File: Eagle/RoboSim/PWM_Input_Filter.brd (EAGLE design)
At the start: 74.6 x 78.7 mm, 66 parts, among them IC1 TLV2772, IC2 TLV2772, IC3 TLV2772

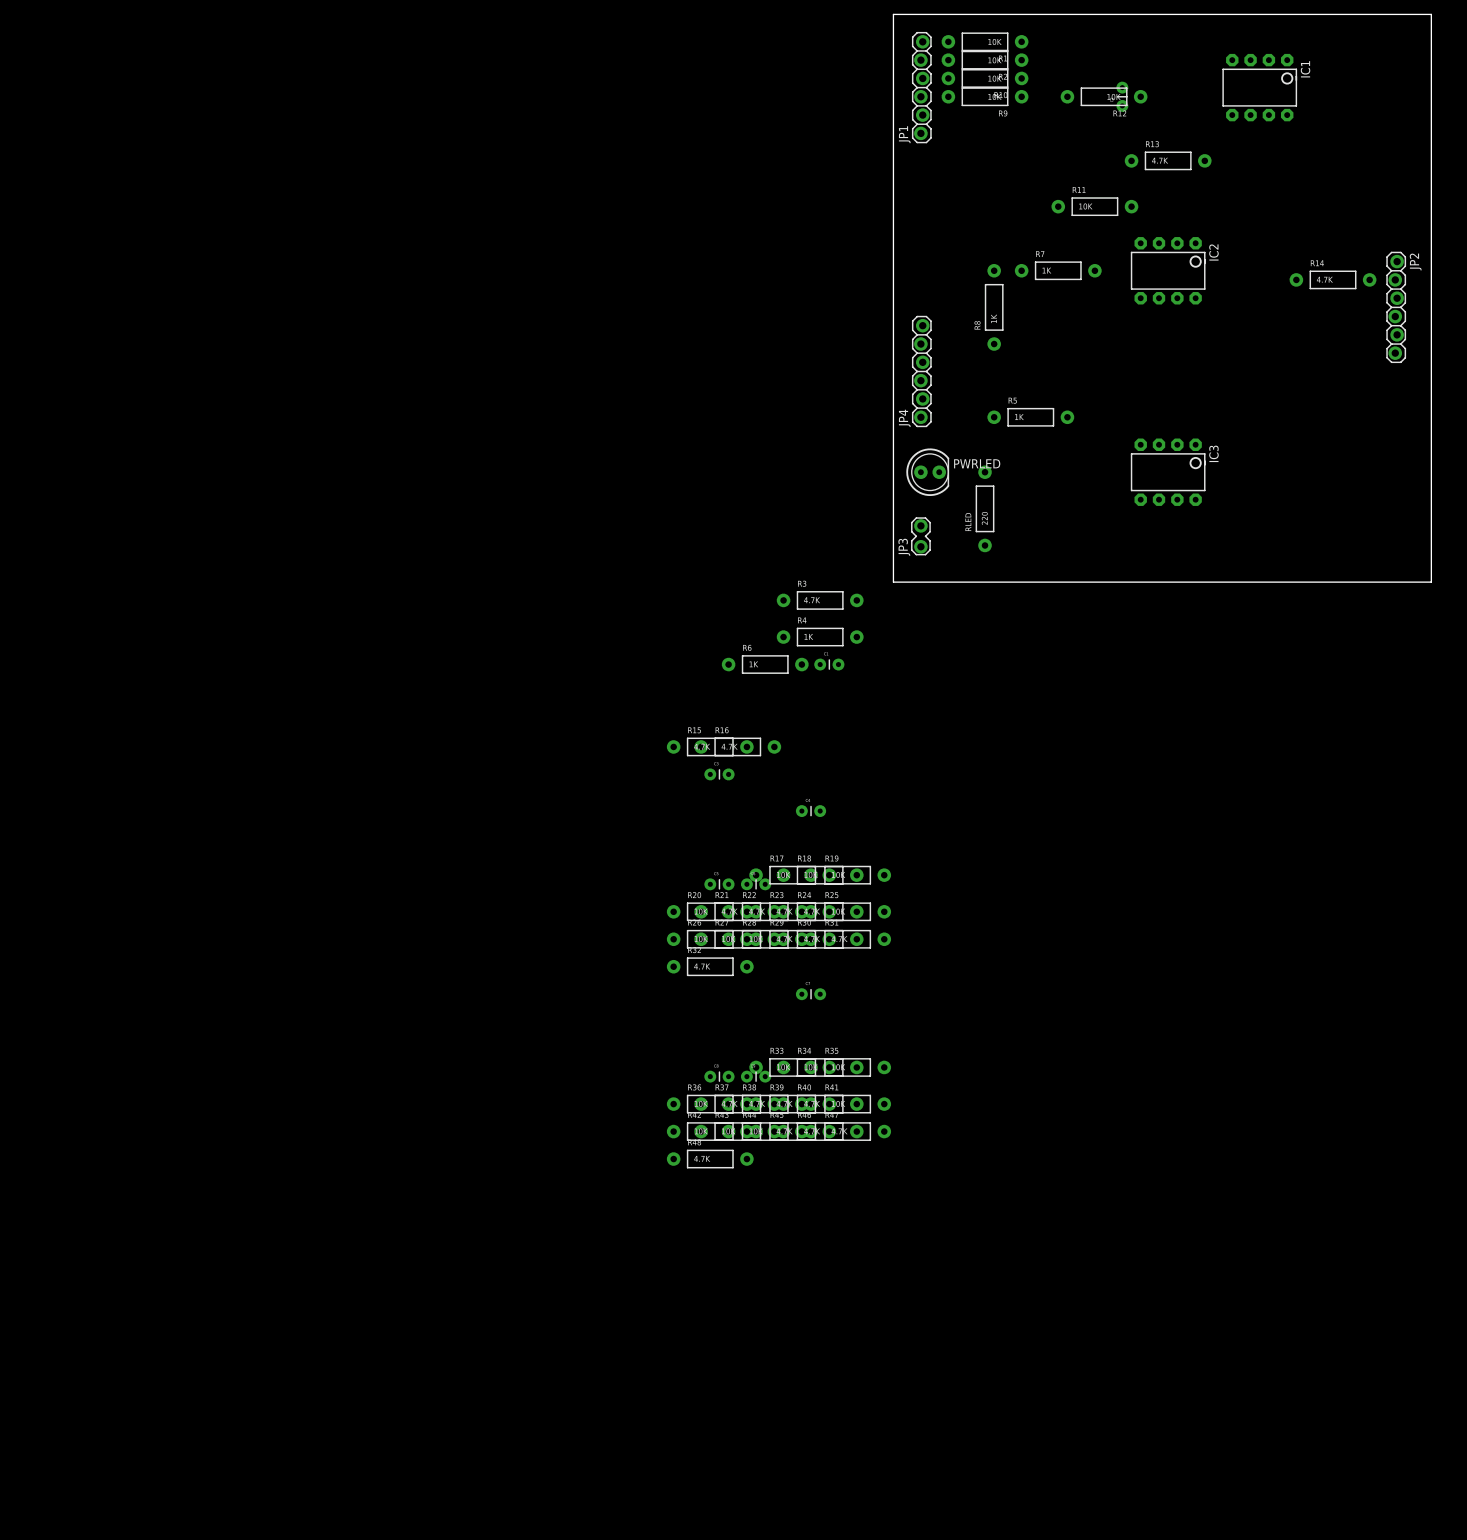
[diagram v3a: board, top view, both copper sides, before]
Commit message: updated resistor values and op-amp configuration
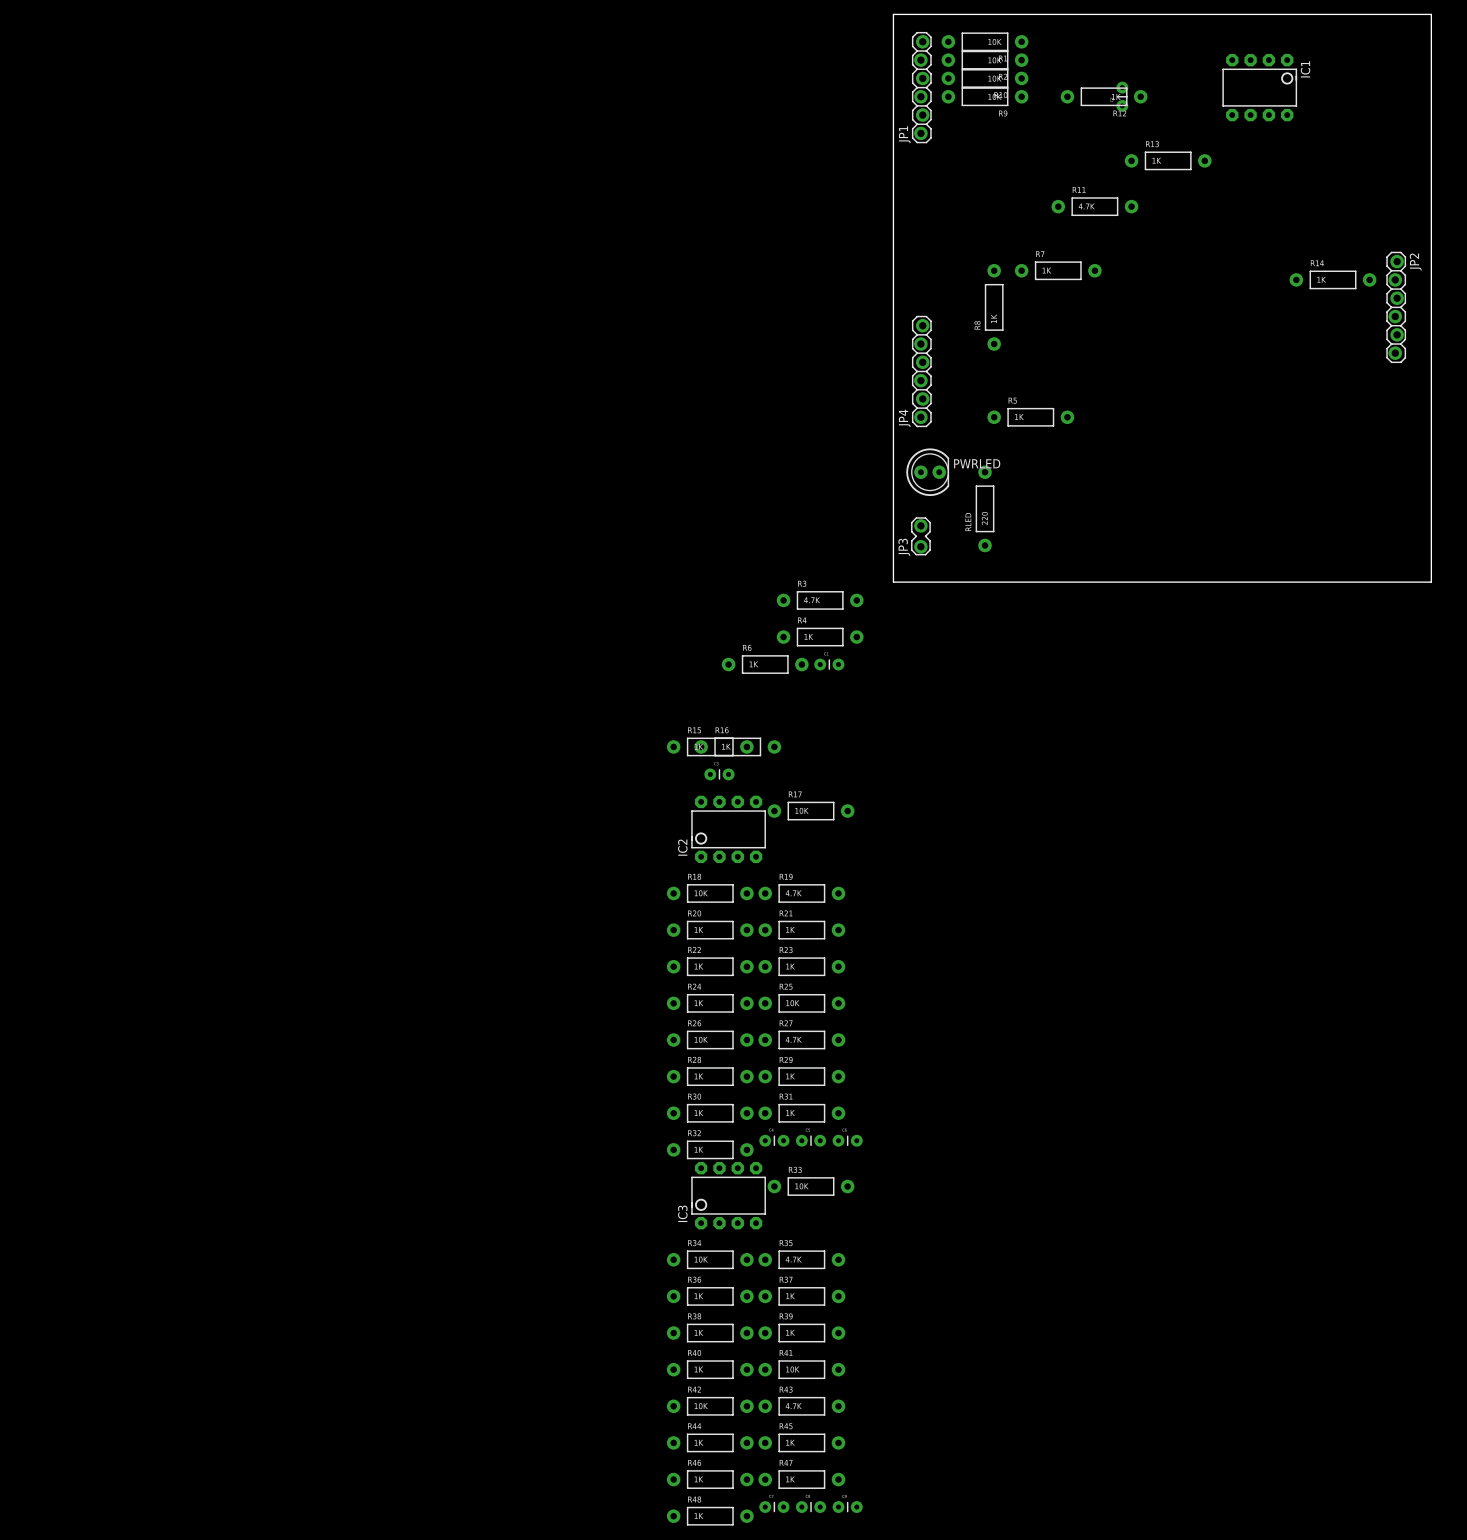
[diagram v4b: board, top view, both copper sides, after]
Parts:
- C2, C4, C7: value 100uF -> 3.7uF
- R11, R19, R27, R35, R43: value 10K -> 4.7K
- R12, R20, R28, R36, R44: value 10K -> 1K
- R13, R14, R15, R16, R21, R22, R23, R24, R29, R30, R31, R32, R37, R38, R39, R40, R45, R46, R47, R48: value 4.7K -> 1K
- moved IC3 117.4 mm to (-22.9, -85.1), turned to 0 degrees
- moved IC2 98.6 mm to (-22.9, -34.3), turned to 0 degrees
- moved C7 71.3 mm to (-17.8, -128.3)
- moved C8 61.0 mm to (-12.7, -128.3)
- moved C9 61.0 mm to (-7.62, -128.3)
- moved R46 50.6 mm to (-25.4, -124.5)
- moved R48 49.5 mm to (-25.4, -129.5)
- moved R47 48.7 mm to (-12.7, -124.5)
- moved C4 46.0 mm to (-17.8, -77.5)
- moved R44 43.8 mm to (-25.4, -119.4)
- moved R45 43.2 mm to (-12.7, -119.4)
- moved R40 39.9 mm to (-25.4, -109.2)
- moved R43 39.1 mm to (-12.7, -114.3)
- moved R42 38.1 mm to (-25.4, -114.3)
- moved C5 37.8 mm to (-12.7, -77.5)
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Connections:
- removed net N$26 (its old number): IC2.5, R26.P$1, R27.P$2, R29.P$1
- removed net N$27 (its old number): IC2.6, R25.P$1, R28.P$2, R31.P$2
- removed net N$32 (its old number): JP4.3, R33.P$2
- removed net N$40 (its old number): IC3.5, R42.P$1, R43.P$2, R45.P$1
- removed net N$41 (its old number): IC3.6, R41.P$1, R44.P$2, R47.P$2
- new net N$28: IC2.6, R26.P$1, R27.P$2, R29.P$1
- new net N$29: IC2.5, R25.P$1, R28.P$2, R31.P$2
- new net N$31: R33.P$2
- new net N$48: IC3.6, R42.P$1, R43.P$2, R45.P$1
- new net N$49: IC3.5, R41.P$1, R44.P$2, R47.P$2
- net N$11: now also IC1.6; no longer IC1.5
- net N$12: now also IC1.5; no longer IC1.6
- net N$16: now also R18.P$2; no longer R17.P$2
- net N$2: now also R17.P$2; no longer R18.P$2

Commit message: changed pins to screw terminals and made resistors surface mount. Still need to position components and route
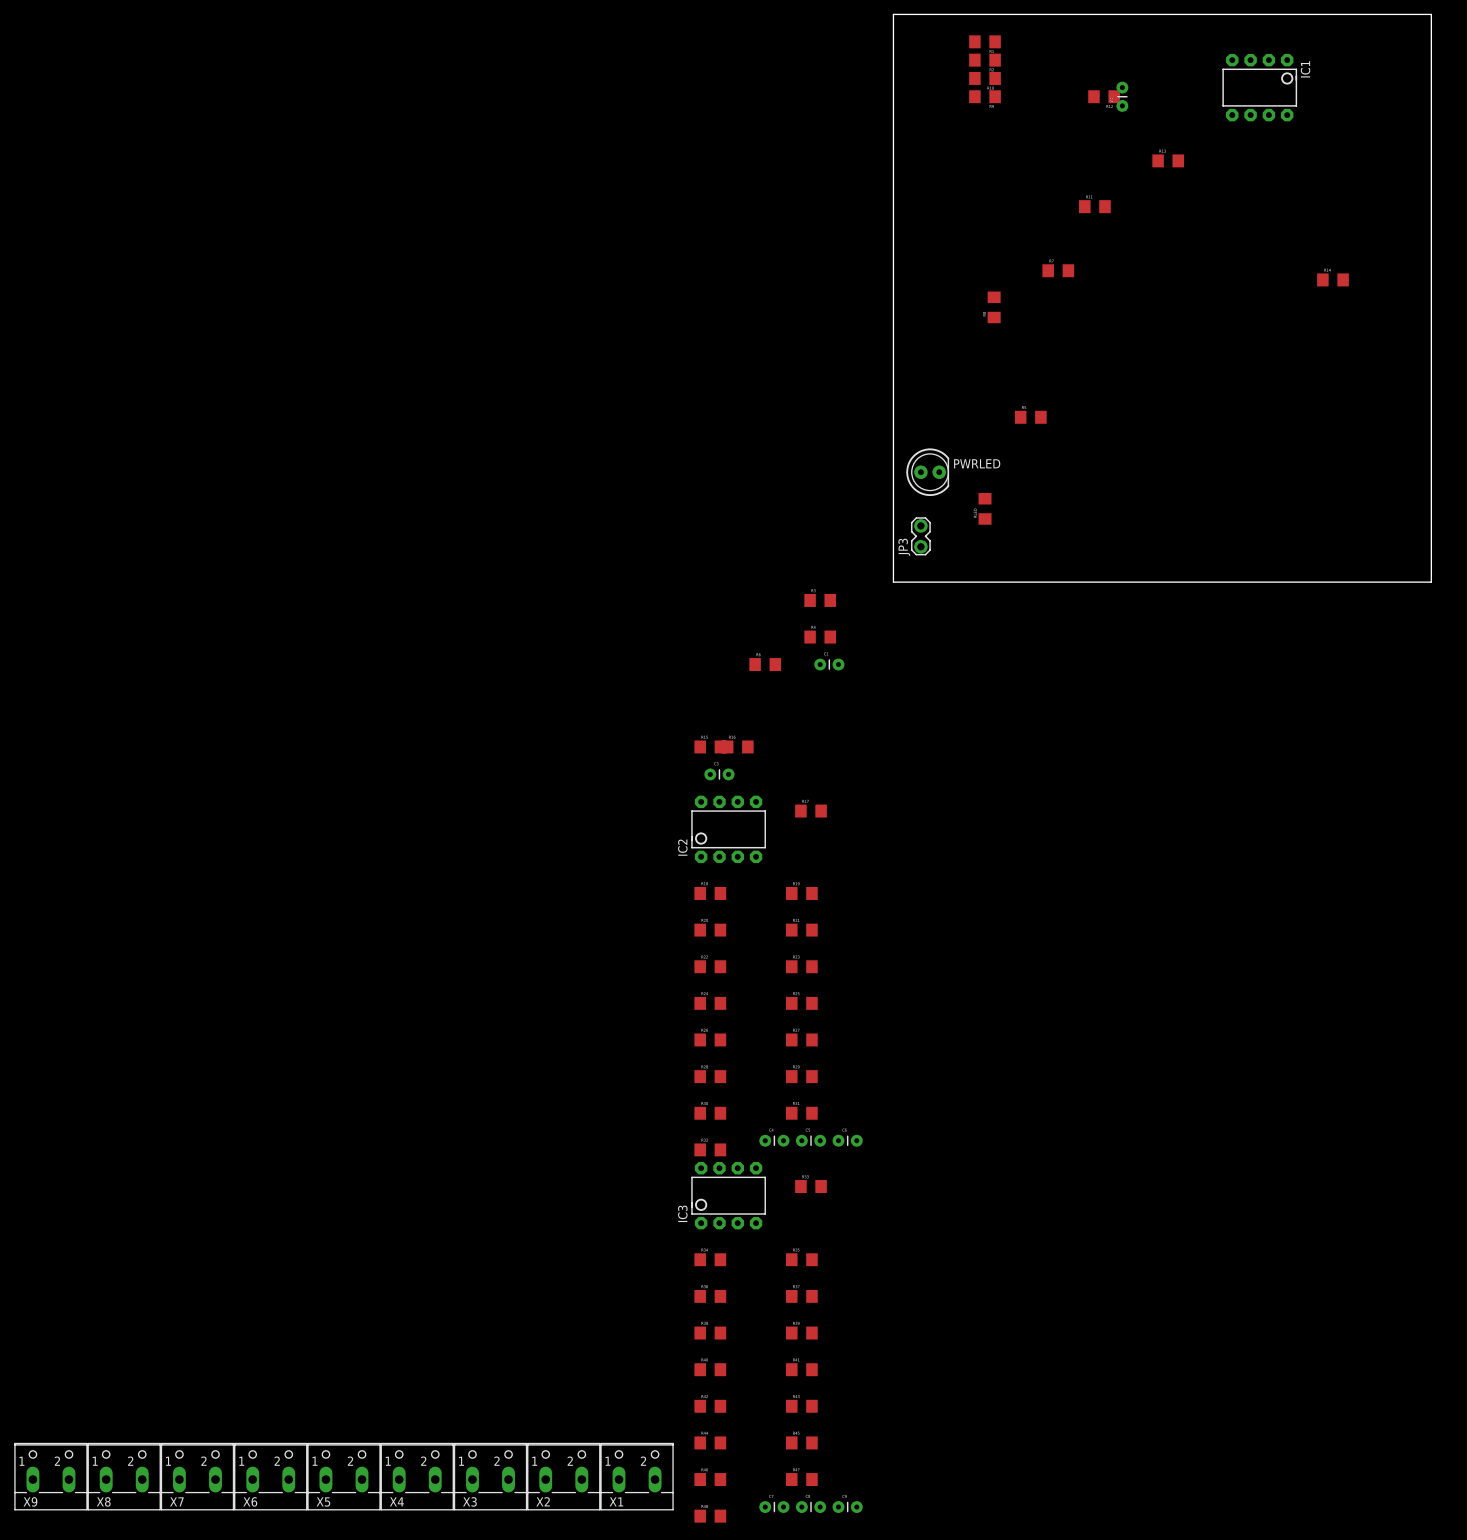
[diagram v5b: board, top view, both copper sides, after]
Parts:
- removed JP1, JP2, JP4: (no value), SparkFun-Connectors:1X06_LOCK
- added X1, X2, X3, X4, X5, X6, X7, X8, X9: (no value), con-wago-500:W237-102
- R1, R10, R11, R12, R13, R14, R15, R16, R17, R18, R19, R2, R20, R21, R22, R23, R24, R25, R26, R27, R28, R29, R3, R30, R31, R32, R33, R34, R35, R36, R37, R38, R39, R4, R40, R41, R42, R43, R44, R45, R46, R47, R48, R5, R6, R7, R8, R9, RLED: device SparkFun-Passives:AXIAL-0.4 -> SparkFun-Passives:1206
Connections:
- removed net N$42: JP4.1, R41.P$2
- new net N$34: R41.2, X6.2
- net GND: now also R16.1, R24.1, R32.1, R40.1, R48.1, R8.1, RLED.1; no longer R16.P$1, R24.P$1, R32.P$1, R40.P$1, R48.P$1, R8.P$1, RLED.P$1
- net N$1: now also R1.2, X1.1; no longer JP1.6, R1.P$2
- net N$10: now also R7.1, R8.2; no longer R7.P$1, R8.P$2
- net N$11: now also R10.1, R11.2, R13.1; no longer R10.P$1, R11.P$2, R13.P$1
- net N$12: now also R12.2, R15.2, R9.1; no longer R12.P$2, R15.P$2, R9.P$1
- net N$13: now also R14.2, X7.1; no longer JP2.2, R14.P$2
- net N$14: now also R10.2, X2.1; no longer JP1.4, R10.P$2
- net N$15: now also R13.2, R14.1; no longer R13.P$2, R14.P$1
- net N$16: now also R18.2, X3.2; no longer JP1.1, R18.P$2
- net N$17: now also R15.1, R16.2; no longer R15.P$1, R16.P$2
- net N$18: now also R30.2, X8.1; no longer JP2.4, R30.P$2
- net N$2: now also R17.2, X3.1; no longer JP1.2, R17.P$2
- net N$20: now also R25.2, X4.2; no longer JP4.5, R25.P$2
- net N$21: now also R9.2, X2.2; no longer JP1.3, R9.P$2
- net N$22: now also R26.2, X4.1; no longer JP4.6, R26.P$2
- net N$24: now also R18.1, R19.2, R21.1; no longer R18.P$1, R19.P$2, R21.P$1
- net N$25: now also R17.1, R20.2, R23.2; no longer R17.P$1, R20.P$2, R23.P$2
- net N$26: now also R21.2, R22.1; no longer R21.P$2, R22.P$1
- net N$27: now also R23.1, R24.2; no longer R23.P$1, R24.P$2
- net N$28: now also R26.1, R27.2, R29.1; no longer R26.P$1, R27.P$2, R29.P$1
- net N$29: now also R25.1, R28.2, R31.2; no longer R25.P$1, R28.P$2, R31.P$2
- net N$30: now also R34.2, X5.1; no longer JP4.4, R34.P$2
- net N$31: now also R33.2, X5.2; no longer R33.P$2
- net N$32: now also R29.2, R30.1; no longer R29.P$2, R30.P$1
- net N$36: now also R31.1, R32.2; no longer R31.P$1, R32.P$2
- net N$37: now also R22.2, X8.2; no longer JP2.3, R22.P$2
- net N$40: now also R46.2, X9.1; no longer JP2.6, R46.P$2
- net N$41: now also R42.2, X6.1; no longer JP4.2, R42.P$2
- net N$43: now also R34.1, R35.2, R37.1; no longer R34.P$1, R35.P$2, R37.P$1
- net N$44: now also R6.2, X7.2; no longer JP2.1, R6.P$2
- net N$45: now also R33.1, R36.2, R39.2; no longer R33.P$1, R36.P$2, R39.P$2
- net N$46: now also R37.2, R38.1; no longer R37.P$2, R38.P$1
- net N$47: now also R39.1, R40.2; no longer R39.P$1, R40.P$2
- net N$48: now also R42.1, R43.2, R45.1; no longer R42.P$1, R43.P$2, R45.P$1
- net N$49: now also R41.1, R44.2, R47.2; no longer R41.P$1, R44.P$2, R47.P$2
- net N$5: now also RLED.2; no longer RLED.P$2
- net N$50: now also R45.2, R46.1; no longer R45.P$2, R46.P$1
- net N$51: now also R47.1, R48.2; no longer R47.P$1, R48.P$2
- net N$52: now also R38.2, X9.2; no longer JP2.5, R38.P$2
- net N$6: now also R1.1, R3.2, R5.1; no longer R1.P$1, R3.P$2, R5.P$1
- net N$7: now also R2.1, R4.2, R7.2; no longer R2.P$1, R4.P$2, R7.P$2
- net N$8: now also R2.2, X1.2; no longer JP1.5, R2.P$2
- net N$9: now also R5.2, R6.1; no longer R5.P$2, R6.P$1
- net VCC: now also R11.1, R12.1, R19.1, R20.1, R27.1, R28.1, R3.1, R35.1, R36.1, R4.1, R43.1, R44.1; no longer R11.P$1, R12.P$1, R19.P$1, R20.P$1, R27.P$1, R28.P$1, R3.P$1, R35.P$1, R36.P$1, R4.P$1, R43.P$1, R44.P$1
